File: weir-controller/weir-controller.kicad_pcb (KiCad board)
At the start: 4 copper layers, 93 x 60.1 mm, 52 parts, among them J1 Screw_Terminal_01x02, J2 Screw_Terminal_01x04, J3 Screw_Terminal_01x04, J4 USB_B_Mini, J5 Wurth_74980104400, J6 Screw_Terminal_01x02, Q1 PSMN0R7-25YLD, Q2 PSMN0R7-25YLD, Q3 PSMN0R7-25YLD, Q4 PSMN0R7-25YLD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

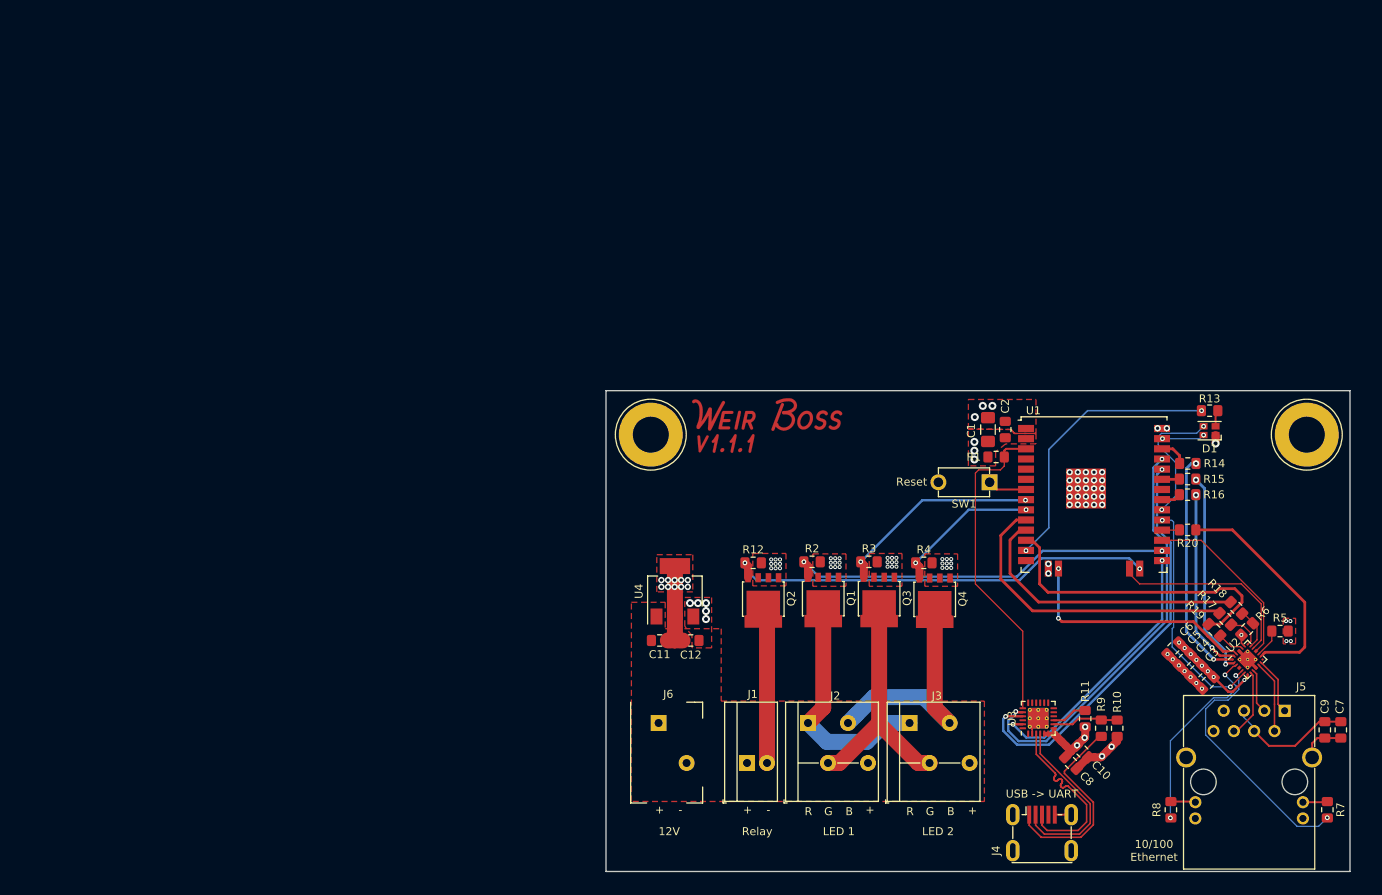
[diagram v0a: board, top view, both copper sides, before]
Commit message: Impedance match the MDI
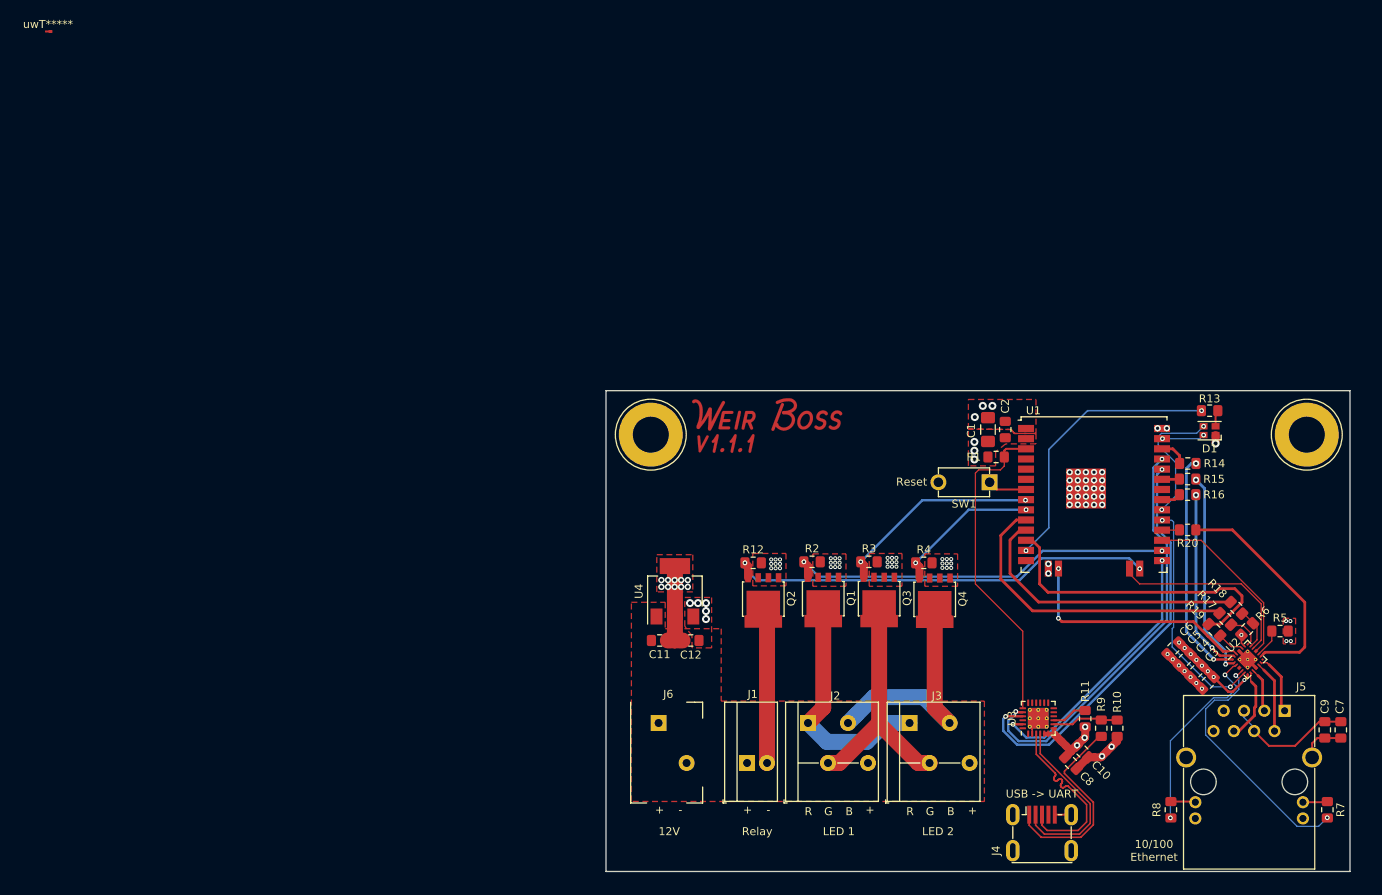
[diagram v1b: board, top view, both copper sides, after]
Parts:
- added uwT*****: uwT0.20_0.20_0.35_0.35_0.50, uwT0.20_0.20_0.35_0.35_0.50, F.Cu at (0.00, 0.00)
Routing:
- net /RD_P: track 5.61 -> 6.12 mm
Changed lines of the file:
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@@
     (thickness 1.6)
     (drawings 23)
-    (tracks 575)
+    (tracks 588)
     (zones 0)
-    (modules 52)
+    (modules 53)
     (nets 68)
   )
@@
     (add_net "Net-(U3-Pad24)")
   )
+  (module uwT0.20_0.20_0.35_0.35_0.50 (layer F.Cu)
+    (at 0 0)
+    (attr virtual)
+    (fp_text reference uwT***** (at 0.25 -0.9) (layer F.SilkS)
+      (effects (font (size 1 1) (thickness 0.15)))
+    )
+    (fp_text value uwT0.20_0.20_0.35_0.35_0.50 (at 0.25 1.4) (layer F.Fab)
+      (effects (font (size 1 1) (thickness 0.15)))
+    )
+    (pad 1 smd custom (at 0 0) (size 0.2 0.2) (layers F.Cu)
+      (zone_connect 0)
+      (options (clearance outline) (anchor rect))
+      (primitives
+        (gr_poly (pts
+           (xy -0.1 -0.1) (xy 0.1 -0.1) (xy 0.425 -0.175) (xy 0.775 -0.175) (xy 0.775 0.175)
+           (xy 0.425 0.175) (xy 0.1 0.1) (xy -0.1 0.1)) (width 0))
+      ))
+    (pad 1 smd rect (at 0.6 0) (size 0.35 0.35) (layers F.Cu))
+  )
   (module custom-parts:4MM_Mounting_Hole (layer F.Cu)
     (at 157.6 50.4)
@@
   (segment (start 149.425216 75.424784) (end 149.425216 76.452423) (width 0.2) (layer F.Cu) (net 1))
   (segment (start 149.425216 75.424784) (end 149.425216 75.424784) (width 0.2) (layer F.Cu) (net 1))
-  (segment (start 150.2 80.664348) (end 150.2 80.373833) (width 0.3) (layer F.Cu) (net 1))
   (segment (start 147.784301 82.5263) (end 148.338048 82.5263) (width 0.3) (layer F.Cu) (net 1))
   (segment (start 145.950161 80.69216) (end 147.784301 82.5263) (width 0.3) (layer F.Cu) (net 1))
@@
   (segment (start 151.69235 77.691918) (end 151.69235 79.18765) (width 0.3) (layer In1.Cu) (net 1))
   (segment (start 148.338048 82.5263) (end 149.802174 81.062174) (width 0.3) (layer F.Cu) (net 1))
-  (segment (start 149.802174 81.062174) (end 150.2 80.664348) (width 0.3) (layer F.Cu) (net 1))
   (via (at 149.802174 81.062174) (size 0.508) (drill 0.254) (layers F.Cu B.Cu) (net 1))
   (segment (start 151.676698 79.18765) (end 149.802174 81.062174) (width 0.3) (layer In1.Cu) (net 1))
   (segment (start 151.69235 79.18765) (end 151.676698 79.18765) (width 0.3) (layer In1.Cu) (net 1))
+  (segment (start 150.2 80.664348) (end 150.2 80.373833) (width 0.3) (layer F.Cu) (net 1))
+  (segment (start 149.802174 81.062174) (end 150.2 80.664348) (width 0.3) (layer F.Cu) (net 1))
   (via (at 144.491933 82.133067) (size 0.508) (drill 0.254) (layers F.Cu B.Cu) (net 2))
   (via (at 140.1 49.6) (size 0.8) (drill 0.4) (layers F.Cu B.Cu) (net 2))
@@
   (segment (start 143.175 54) (end 142.55 54.625) (width 0.348632) (layer B.Cu) (net 31))
   (segment (start 143.75 54) (end 143.175 54) (width 0.348632) (layer B.Cu) (net 31))
-  (segment (start 151.914735 78.906586) (end 154.011 81.002851) (width 0.2) (layer F.Cu) (net 32))
-  (segment (start 151.879379 78.906586) (end 151.914735 78.906586) (width 0.2) (layer F.Cu) (net 32))
-  (segment (start 154.011 84.09) (end 154.831 84.91) (width 0.2) (layer F.Cu) (net 32))
-  (segment (start 154.011 81.002851) (end 154.011 84.09) (width 0.2) (layer F.Cu) (net 32))
-  (segment (start 151.325 83.944) (end 152.291 84.91) (width 0.2) (layer F.Cu) (net 33))
-  (segment (start 151.325 80.296751) (end 151.325 83.944) (width 0.2) (layer F.Cu) (net 33))
-  (segment (start 150.889429 79.896536) (end 150.924785 79.896536) (width 0.2) (layer F.Cu) (net 33))
-  (segment (start 150.924785 79.896536) (end 151.325 80.296751) (width 0.2) (layer F.Cu) (net 33))
-  (segment (start 153.561 81.189249) (end 153.561 84.09) (width 0.2) (layer F.Cu) (net 34))
-  (segment (start 151.596536 79.224785) (end 153.561 81.189249) (width 0.2) (layer F.Cu) (net 34))
-  (segment (start 153.561 84.09) (end 153.561 87.45) (width 0.2) (layer F.Cu) (net 34))
-  (segment (start 151.596536 79.189429) (end 151.596536 79.224785) (width 0.2) (layer F.Cu) (net 34))
-  (segment (start 148.86 87.45) (end 148.481 87.45) (width 0.2) (layer F.Cu) (net 35))
-  (segment (start 150.875 85.435) (end 148.86 87.45) (width 0.2) (layer F.Cu) (net 35))
-  (segment (start 150.875 80.483149) (end 150.875 85.435) (width 0.2) (layer F.Cu) (net 35))
-  (segment (start 150.606586 80.214735) (end 150.875 80.483149) (width 0.2) (layer F.Cu) (net 35))
-  (segment (start 150.606586 80.179379) (end 150.606586 80.214735) (width 0.2) (layer F.Cu) (net 35))
+  (segment (start 152.646586 78.906586) (end 152.87 79.13) (width 0.1524) (layer F.Cu) (net 32))
+  (segment (start 151.879379 78.906586) (end 152.646586 78.906586) (width 0.1524) (layer F.Cu) (net 32))
+  (segment (start 154.411 80.671) (end 152.87 79.13) (width 0.35) (layer F.Cu) (net 32))
+  (segment (start 154.411 84.49) (end 154.411 80.671) (width 0.35) (layer F.Cu) (net 32))
+  (segment (start 154.831 84.91) (end 154.411 84.49) (width 0.35) (layer F.Cu) (net 32))
+  (segment (start 151.921 84.54) (end 152.291 84.91) (width 0.3) (layer F.Cu) (net 33))
+  (segment (start 151.082893 80.092893) (end 151.49 80.5) (width 0.1524) (layer F.Cu) (net 33))
+  (segment (start 151.082893 80.09) (end 151.082893 80.092893) (width 0.1524) (layer F.Cu) (net 33))
+  (segment (start 150.889429 79.896536) (end 151.082893 80.09) (width 0.1524) (layer F.Cu) (net 33))
+  (segment (start 152.081 81.091) (end 151.49 80.5) (width 0.35) (layer F.Cu) (net 33))
+  (segment (start 152.081 84.7) (end 152.081 81.091) (width 0.35) (layer F.Cu) (net 33))
+  (segment (start 152.291 84.91) (end 152.081 84.7) (width 0.35) (layer F.Cu) (net 33))
+  (segment (start 152.207107 79.8) (end 152.21 79.8) (width 0.1524) (layer F.Cu) (net 34))
+  (segment (start 151.596536 79.189429) (end 152.207107 79.8) (width 0.1524) (layer F.Cu) (net 34))
+  (segment (start 153.561 81.151) (end 152.21 79.8) (width 0.35) (layer F.Cu) (net 34))
+  (segment (start 153.561 87.45) (end 153.561 81.151) (width 0.35) (layer F.Cu) (net 34))
+  (segment (start 150.57861 80.495305) (end 150.57861 81.20861) (width 0.1524) (layer F.Cu) (net 35))
+  (segment (start 150.605387 80.468528) (end 150.57861 80.495305) (width 0.1524) (layer F.Cu) (net 35))
+  (segment (start 150.605387 80.279138) (end 150.605387 80.468528) (width 0.1524) (layer F.Cu) (net 35))
+  (segment (start 150.57861 80.252361) (end 150.605387 80.279138) (width 0.1524) (layer F.Cu) (net 35))
+  (segment (start 150.57861 80.217008) (end 150.57861 80.252361) (width 0.1524) (layer F.Cu) (net 35))
+  (segment (start 150.57861 81.20861) (end 150.67 81.3) (width 0.1524) (layer F.Cu) (net 35))
+  (segment (start 150.573783 80.212181) (end 150.57861 80.217008) (width 0.1524) (layer F.Cu) (net 35))
+  (segment (start 150.606586 80.179379) (end 150.573783 80.212181) (width 0.1524) (layer F.Cu) (net 35))
+  (segment (start 151.231 81.861) (end 150.67 81.3) (width 0.35) (layer F.Cu) (net 35))
+  (segment (start 151.231 84.357686) (end 151.231 81.861) (width 0.35) (layer F.Cu) (net 35))
+  (segment (start 151.05 84.538686) (end 151.231 84.357686) (width 0.35) (layer F.Cu) (net 35))
+  (segment (start 151.05 85.52) (end 151.05 84.538686) (width 0.35) (layer F.Cu) (net 35))
+  (segment (start 149.12 87.45) (end 151.05 85.52) (width 0.35) (layer F.Cu) (net 35))
+  (segment (start 148.481 87.45) (end 149.12 87.45) (width 0.35) (layer F.Cu) (net 35))
   (segment (start 123.7 99.225) (end 123.7 97.9) (width 0.2) (layer F.Cu) (net 36) (status 20))
   (segment (start 124.28 90.28) (end 130.525 96.525) (width 0.2) (layer F.Cu) (net 36))

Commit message: Project Updates
Final ref of Weir Controller board. Starting Davis Receiver Board. The later only has the PoE power stage captured.
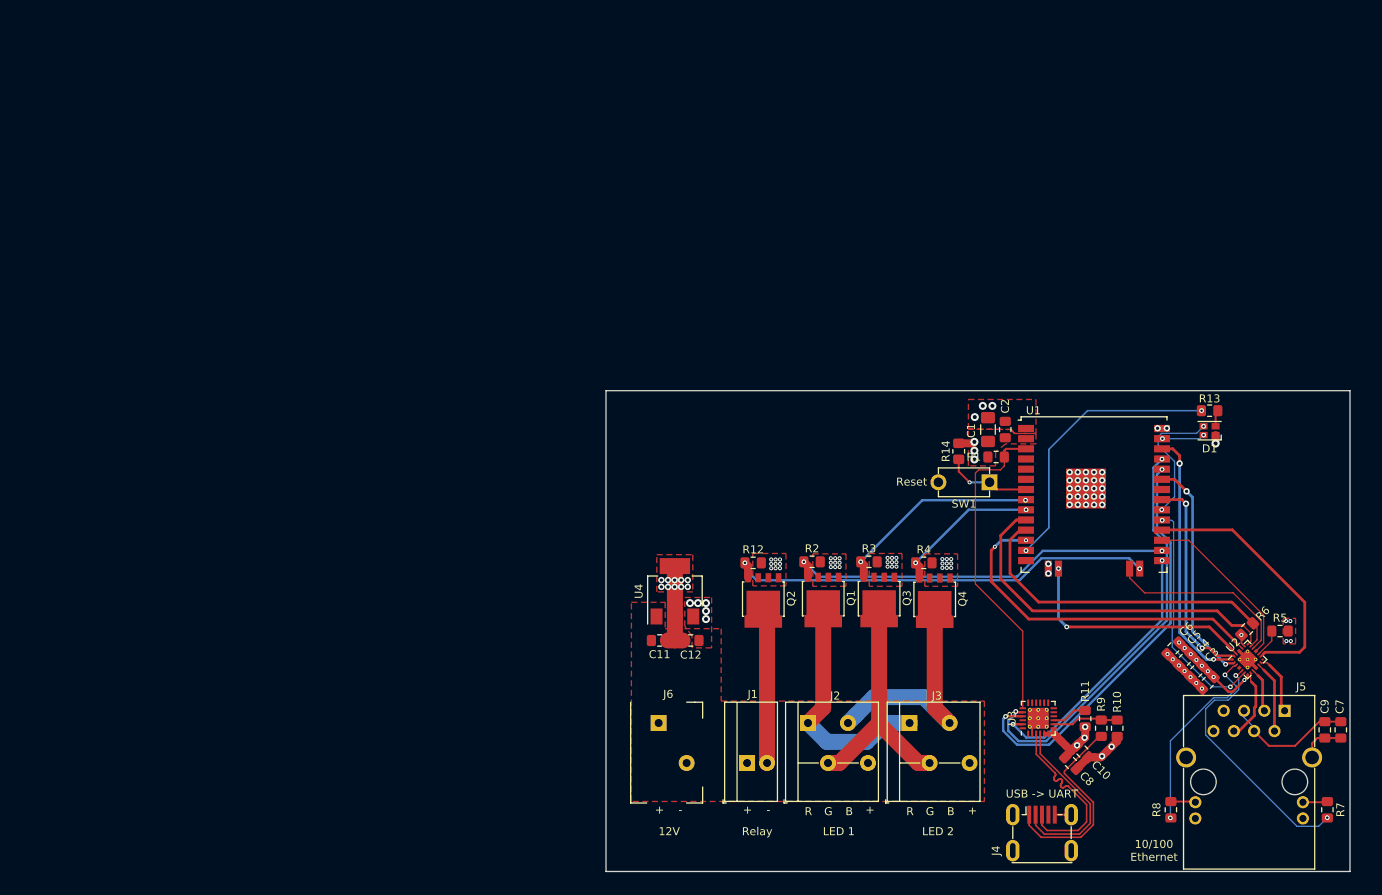
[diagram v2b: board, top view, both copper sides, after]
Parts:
- removed G***: LOGO, custom-parts:v1.1.1_text
- removed G***: LOGO, custom-parts:weir_name_text
- removed R15, R16, R17, R18, R19, R20: 33, Resistor_SMD:R_0805_2012Metric_Pad1.15x1.40mm_HandSolder
- removed REF** (x2): 4MM_Mounting_Hole, custom-parts:4MM_Mounting_Hole
- removed uwT*****: uwT0.20_0.20_0.35_0.35_0.50, uwT0.20_0.20_0.35_0.35_0.50
- R14: value 33 -> 10K; footprint Resistor_SMD:R_0805_2012Metric_Pad1.15x1.40mm_HandSolder -> Resistor_SMD:R_0805_2012Metric_Pad1.20x1.40mm_HandSolder
- moved R14 28.7 mm to (114.1, 52.5), turned to 270 degrees
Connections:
- R14 pad 1: /TX_D1 -> +3V3
- R14 pad 2: Net-(R14-Pad2) -> /FACTORY_RESET
- R6 pad 2: /RX_D1_M -> /RX_D1
- U1 pad 28: Net-(R20-Pad2) -> /PHY_50MHzIn
- U1 pad 31: Net-(R16-Pad1) -> /TX_D0
- U1 pad 33: Net-(R15-Pad1) -> /TX_EN
- U1 pad 36: Net-(R14-Pad2) -> /TX_D1
- U2 pad 12: Net-(U2-Pad12) -> (no net)
- U2 pad 17: /RX_D1_M -> /RX_D1
- U2 pad 18: Net-(R17-Pad2) -> /RX_D0
- U2 pad 20: Net-(R19-Pad1) -> /CRS_DV
- U2 pad 3: Net-(U2-Pad3) -> (no net)
- U3 pad 1: Net-(U3-Pad1) -> (no net)
- U3 pad 10: Net-(U3-Pad10) -> (no net)
- U3 pad 11: Net-(U3-Pad11) -> (no net)
- U3 pad 12: Net-(U3-Pad12) -> (no net)
- U3 pad 13: Net-(U3-Pad13) -> (no net)
- U3 pad 14: Net-(U3-Pad14) -> (no net)
- U3 pad 15: Net-(U3-Pad15) -> (no net)
- U3 pad 16: Net-(U3-Pad16) -> (no net)
- U3 pad 17: Net-(U3-Pad17) -> (no net)
- U3 pad 18: Net-(U3-Pad18) -> (no net)
- U3 pad 22: Net-(U3-Pad22) -> (no net)
- U3 pad 24: Net-(U3-Pad24) -> (no net)
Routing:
- net /RX_D1: track 35.7 -> 42.4 mm
- net /RX_D0: track 38.5 -> 45.1 mm
- net /FACTORY_RESET: track 4.93 -> 10.9 mm, vias 0 -> 1
- net /RX_D1_M: track 5.26 -> 0.00 mm
- net /CRS_DV: track 39.0 -> 43.6 mm, vias 0 -> 2
- net Net-(R17-Pad2): track 4.50 -> 0.00 mm
- net /PHY_50MHzIn: track 28.9 -> 33.2 mm
- net /TX_D1: track 29.1 -> 32.7 mm
- net Net-(R14-Pad2): track 3.53 -> 0.00 mm
- net Net-(R19-Pad1): track 3.39 -> 0.00 mm
- net /TX_D0: track 23.0 -> 26.4 mm
- net /TX_EN: track 25.6 -> 28.4 mm
- net Net-(R16-Pad1): track 2.43 -> 0.00 mm
- net Net-(R20-Pad2): track 2.18 -> 0.00 mm
- net Net-(R15-Pad1): track 2.18 -> 0.00 mm
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
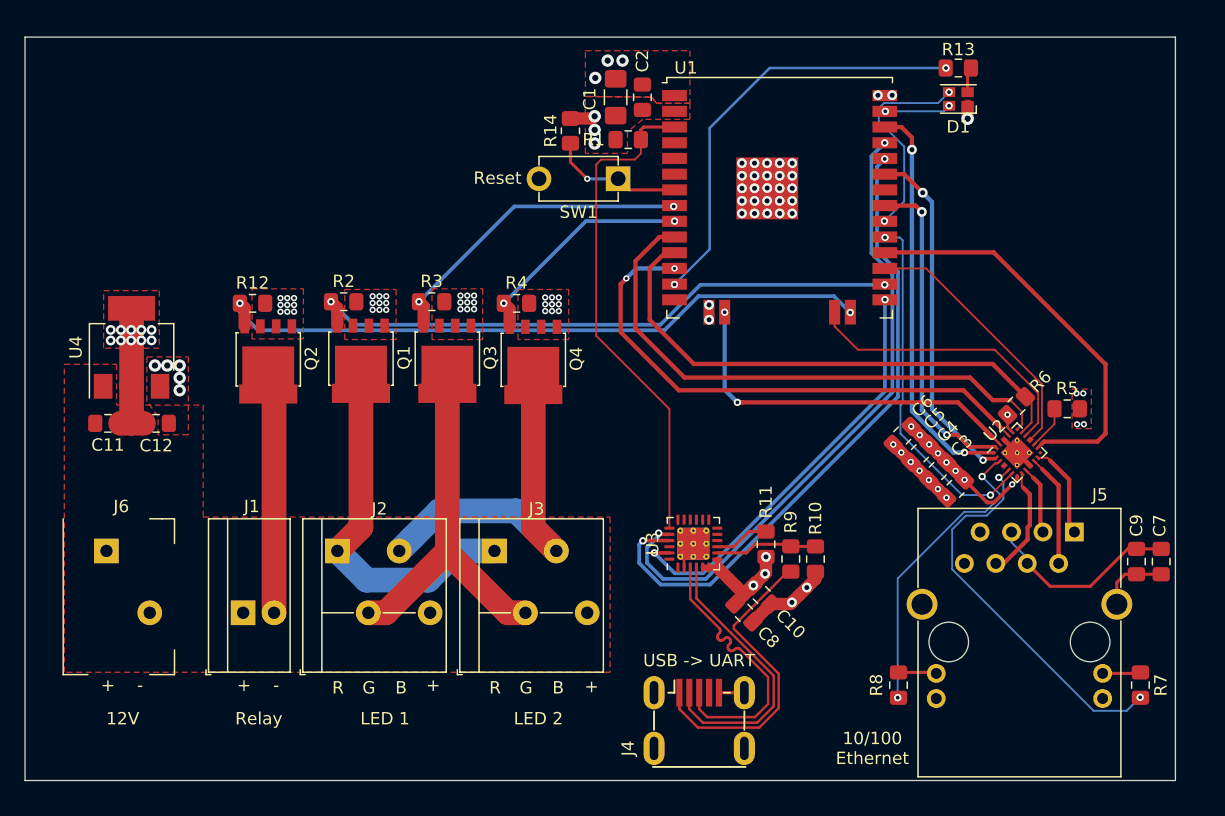
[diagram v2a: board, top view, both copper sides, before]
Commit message: Davis RX and Weir Controller changes
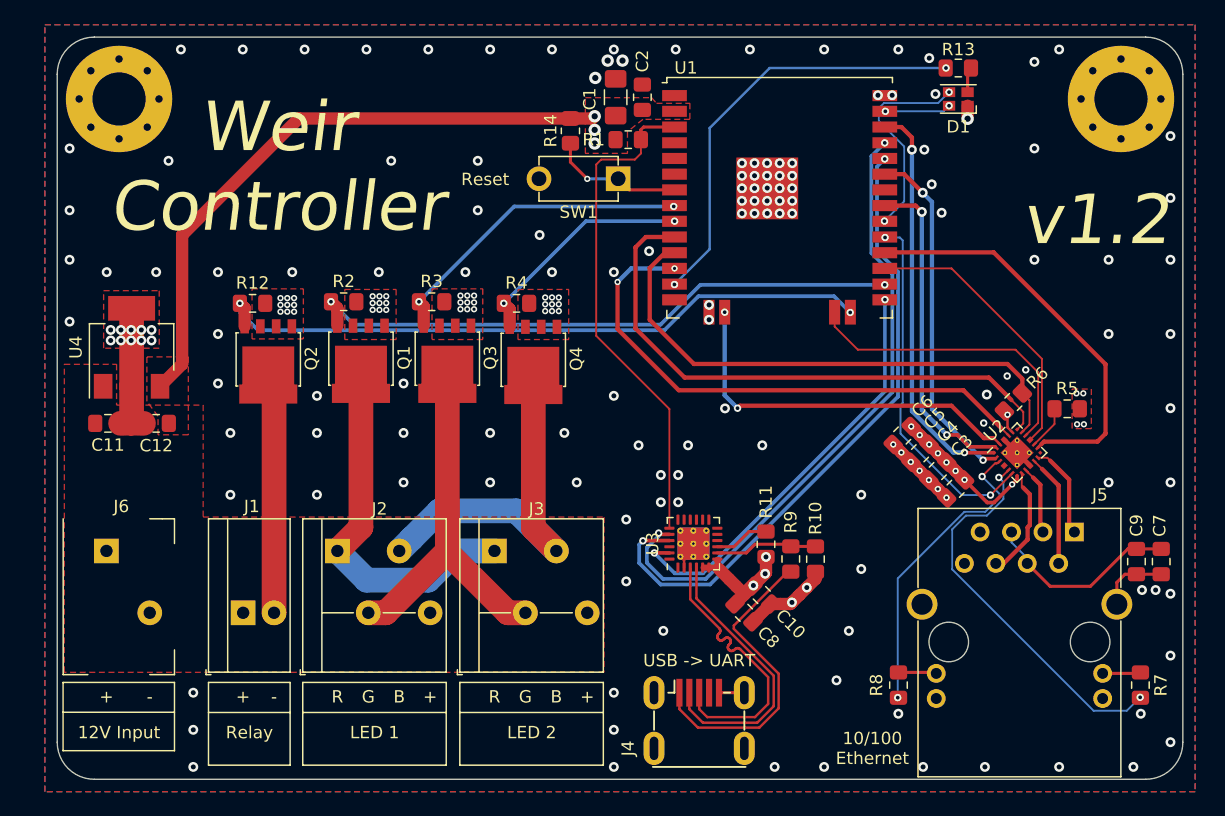
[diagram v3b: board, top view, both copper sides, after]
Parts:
- added REF**: MountingHole_4.3mm_M4_Pad_Via, MountingHole:MountingHole_4.3mm_M4_Pad_Via, F.Cu at (77.6, 49.9)
- added REF**: MountingHole_4.3mm_M4_Pad_Via, MountingHole:MountingHole_4.3mm_M4_Pad_Via, F.Cu at (158.6, 49.9)
- moved R6 0.39 mm to (149.9, 74.4)
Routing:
- net +3V3: track 33.8 -> 217.4 mm, vias 21 -> 16
- net /MDIO: track 21.5 -> 22.7 mm
- net /RX_D1: track 42.4 -> 43.6 mm
- net /MDC: track 23.7 -> 24.7 mm
- net /RX_D0: track 45.1 -> 45.8 mm
- net GND: vias 91 -> 192
- added copper zone on B.Cu, net GND
- added copper zone on In1.Cu, net GND
- removed copper zone on In1.Cu, net +3V3
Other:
- board size 93 x 60.1 mm -> 91 x 60 mm
- net class Default removed
- board text added: "12V Input"
- board text added: "Weir Controller"
- board text added: "v1.2"
- board text removed: "12V"
